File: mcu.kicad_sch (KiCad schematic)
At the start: 28 parts, among them J13 Conn_02x02_Odd_Even, J14 Conn_01x02, SW1 SW_Push, SW2 SW_Push, U1 RP2040, U2 W25Q128JVS, Y1 Crystal_GND24

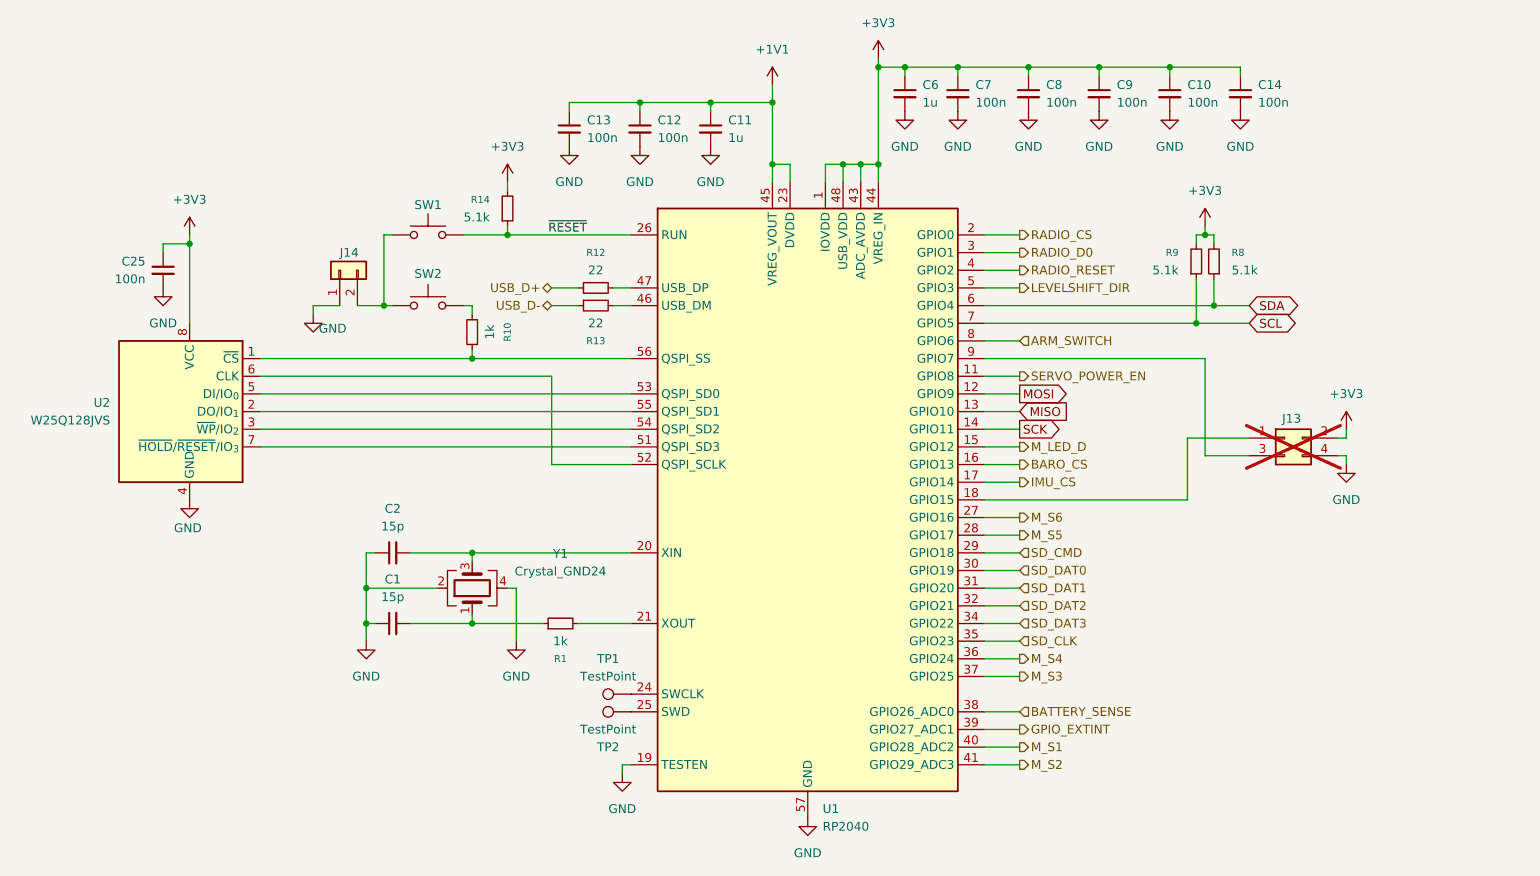
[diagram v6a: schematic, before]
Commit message: add schematic PDF, improve schematic readability
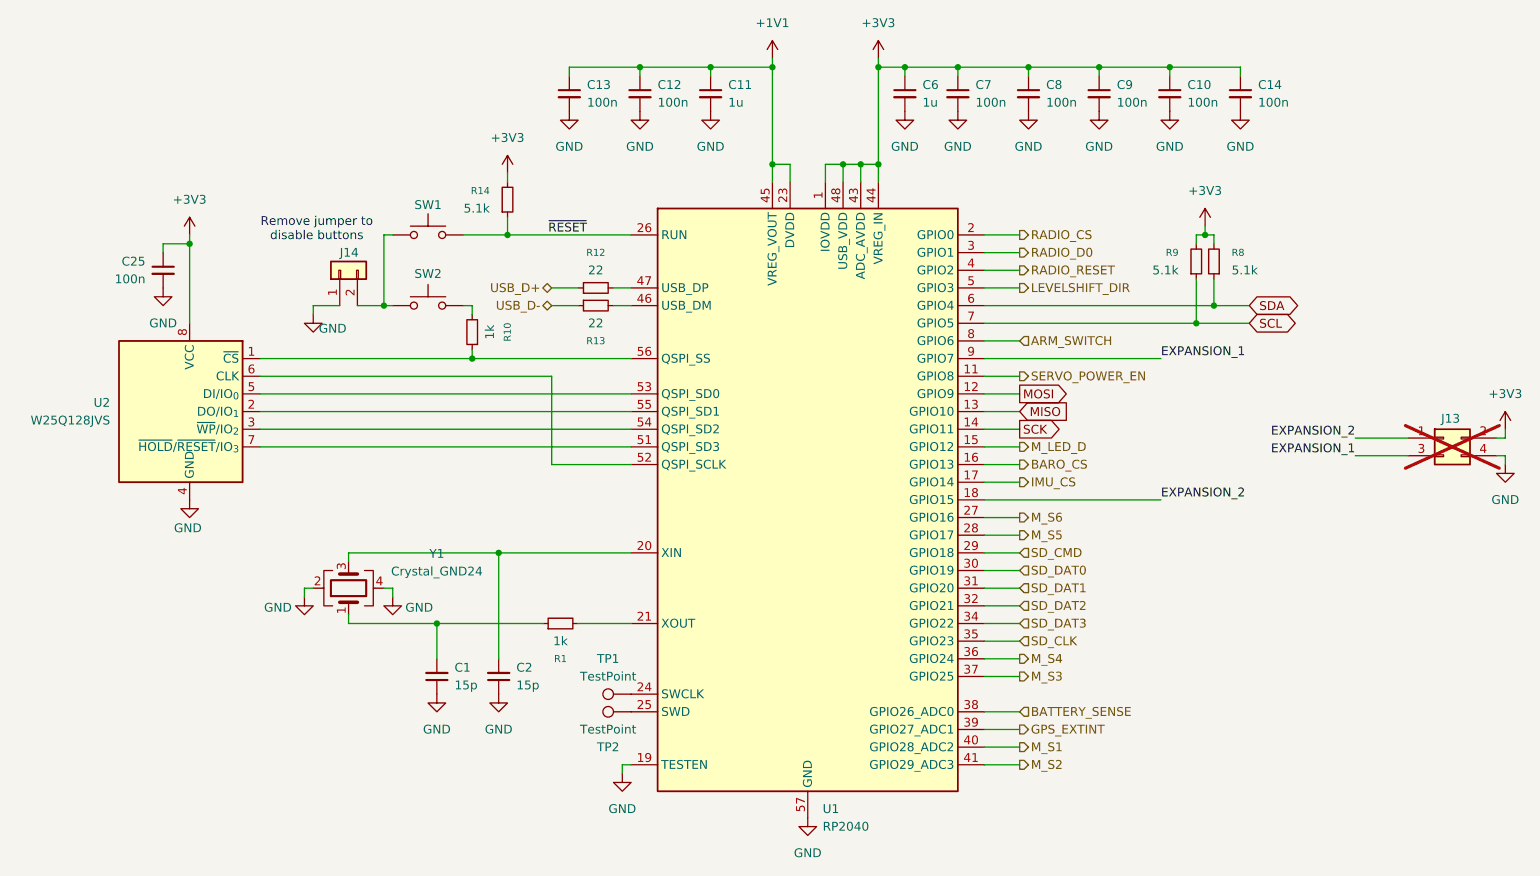
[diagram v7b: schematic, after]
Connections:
- net EXPANSION_2: now reaches J13.1 (Pin_1), U1.18 (GPIO15)
- net EXPANSION_1: now reaches J13.3 (Pin_3), U1.9 (GPIO7)
- net GPIO_EXTINT renamed GPS_EXTINT
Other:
- note added: "Remove jumper to disable buttons"
- moved on the sheet: C1, C11, C12, C13, C2, J13, R14, Y1
